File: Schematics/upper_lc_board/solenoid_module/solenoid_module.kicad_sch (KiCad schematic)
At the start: 16 parts

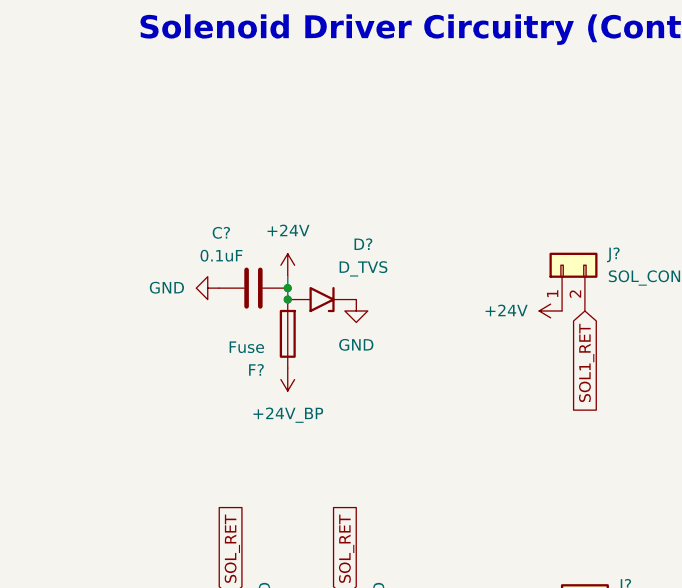
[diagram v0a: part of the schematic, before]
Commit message: update board, add new fuse
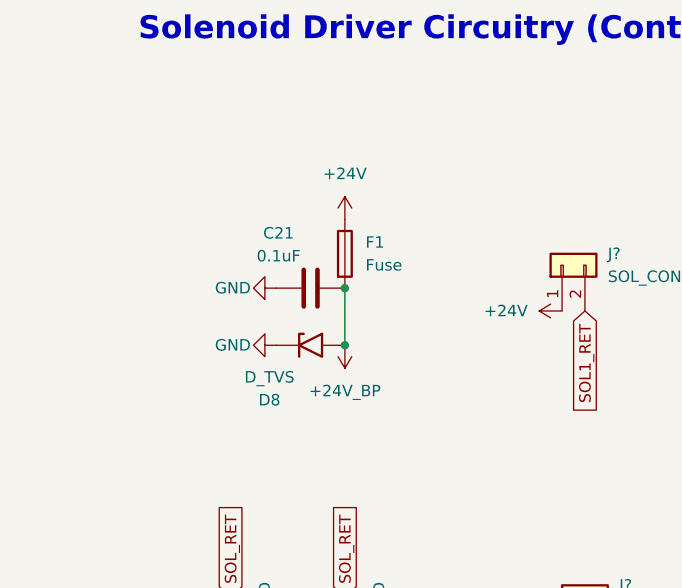
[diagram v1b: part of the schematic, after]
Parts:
- removed C?: 0.1uF, Capacitor_SMD:C_0603_1608Metric, symbol Device:C
- removed D?: D_TVS, SMBJ28A:DIOM5436X244N, symbol Diode:1.5KExxA
- removed F?: Fuse, symbol Device:Fuse
- added C21: 0.1uF, Capacitor_SMD:C_0603_1608Metric, symbol Device:C
- added D8: D_TVS, SMBJ28A:DIOM5436X244N, symbol Diode:1.5KExxA
- added F1: Fuse, symbol Device:Fuse
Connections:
- net +24V: now also F1.1
- net +24V_BP: now also C21.2, D8.2 (A2), F1.2
- net GND: now also C21.1, D8.1 (A1)

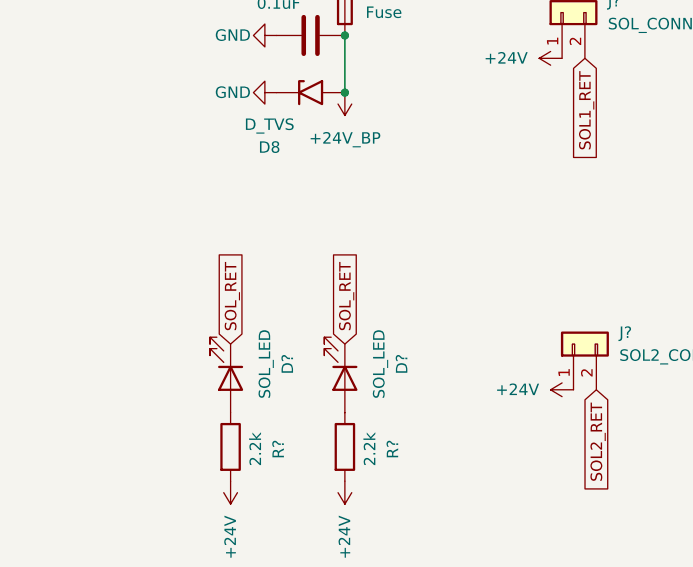
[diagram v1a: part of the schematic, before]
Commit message: update layout with new connector
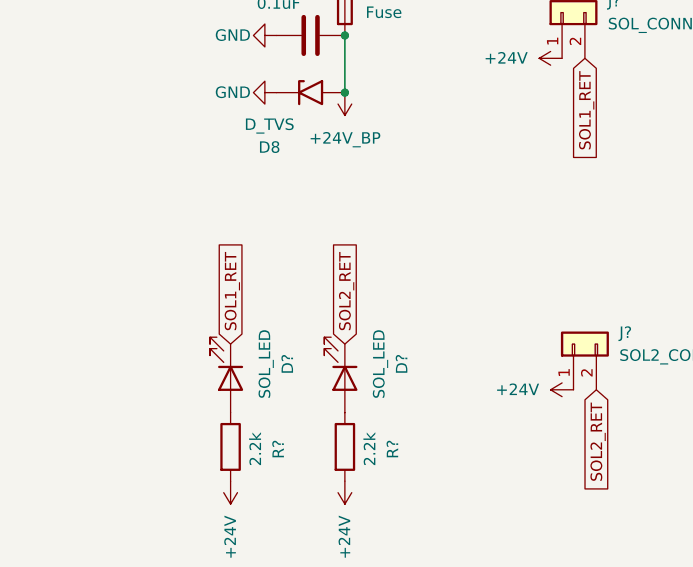
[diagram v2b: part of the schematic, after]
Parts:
- J? (x2): footprint Connector_JST:JST_EH_S2B-EH_1x02_P2.50mm_Horizontal -> 530480210:MOLEX_530480210
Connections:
- net SOL1_RET: now also D?.1 (K)
- net SOL2_RET: now also D?.1 (K)
- removed net SOL_RET: D?.1 (K), D?.1 (K)
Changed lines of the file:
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@@
 		)
 	)
-	(global_label "SOL_RET"
+	(global_label "SOL1_RET"
 		(shape input)
 		(at 25.4 85.09 90)
@@
 		)
 		(property "Intersheetrefs" "${INTERSHEET_REFS}"
-			(at 25.4 74.1825 90)
+			(at 25.4 72.973 90)
 			(effects
 				(font
@@
 		)
 	)
-	(global_label "SOL_RET"
+	(global_label "SOL2_RET"
 		(shape input)
 		(at 38.1 85.09 90)
@@
 		)
 		(property "Intersheetrefs" "${INTERSHEET_REFS}"
-			(at 38.1 74.1825 90)
+			(at 38.1 72.973 90)
 			(effects
 				(font
@@
 			)
 		)
-		(property "Footprint" "Connector_JST:JST_EH_S2B-EH_1x02_P2.50mm_Horizontal"
+		(property "Footprint" "530480210:MOLEX_530480210"
 			(at 62.23 48.26 0)
 			(effects
@@
 			)
 		)
-		(property "Footprint" "Connector_JST:JST_EH_S2B-EH_1x02_P2.50mm_Horizontal"
+		(property "Footprint" "530480210:MOLEX_530480210"
 			(at 63.5 85.09 0)
 			(effects

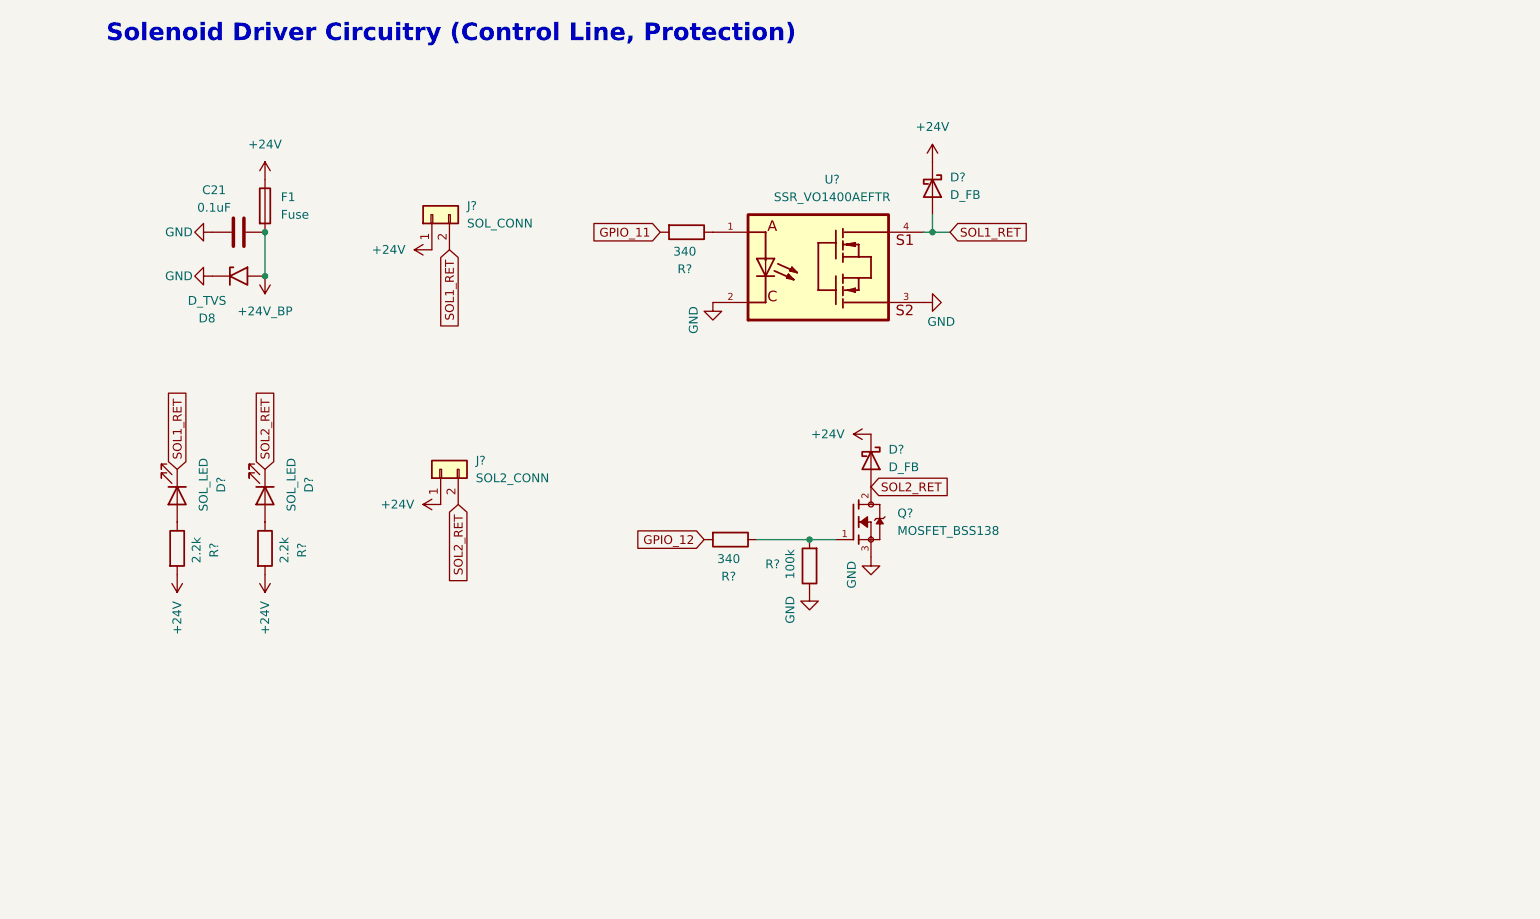
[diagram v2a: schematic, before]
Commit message: start redesigning ADC circuitry, organize schematic files. adding OPAMPS for buffered voltage divider on HALL & on PTs. layout to be adjusted after.
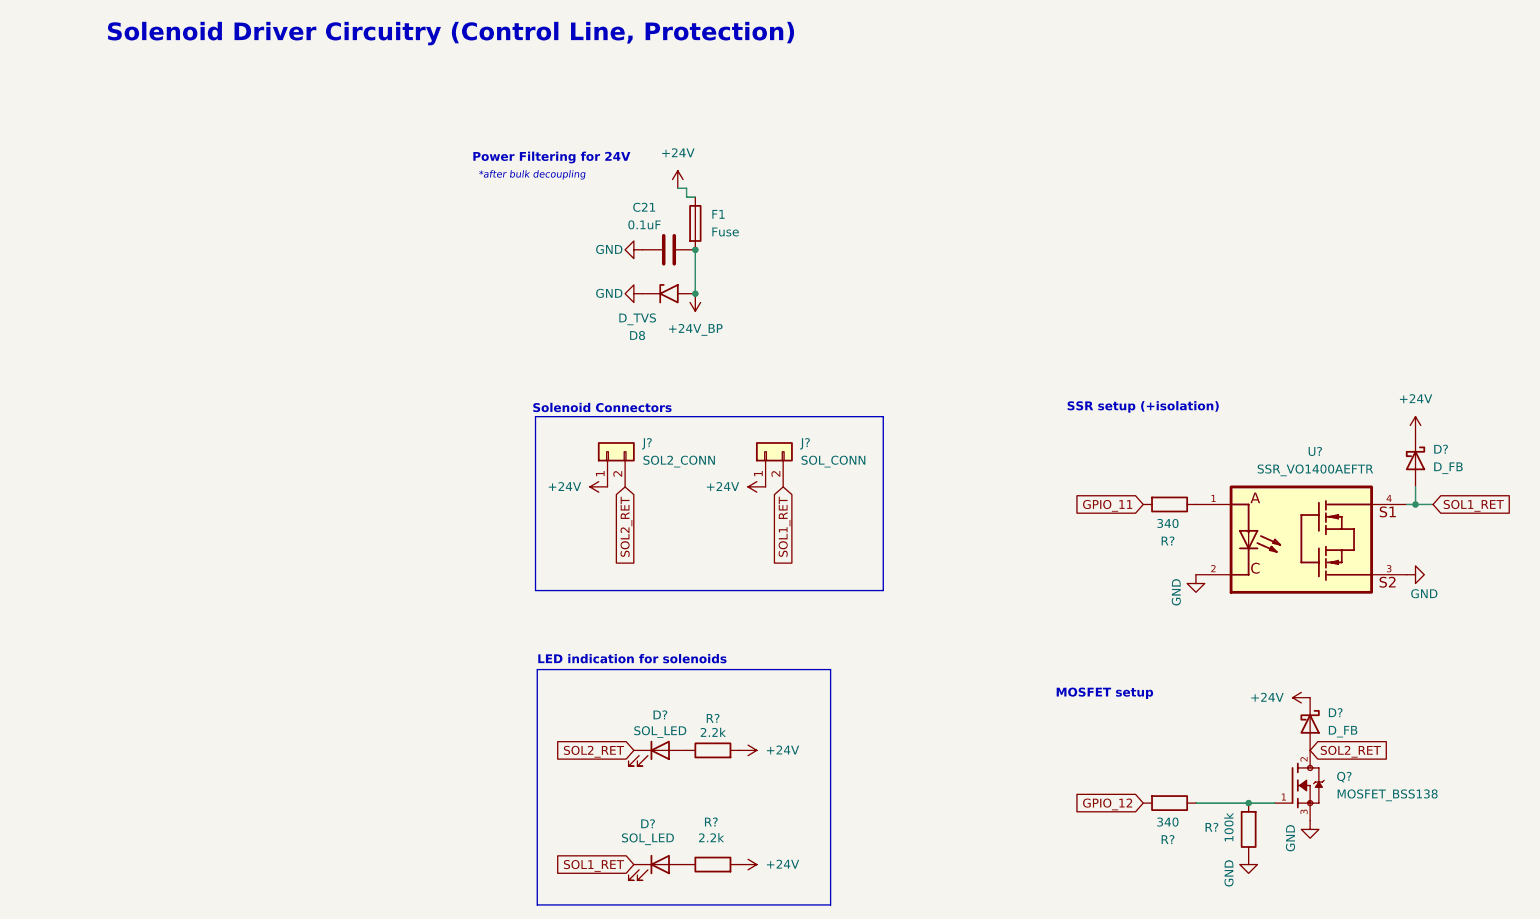
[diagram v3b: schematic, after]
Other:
- note added: "*after bulk decoupling"
- note added: "LED indication for solenoids"
- note added: "MOSFET setup"
- note added: "Power Filtering for 24V"
- note added: "SSR setup (+isolation)"
- note added: "Solenoid Connectors"
- moved on the sheet: C21, D8, D?, F1, J?, Q?, R?, U?

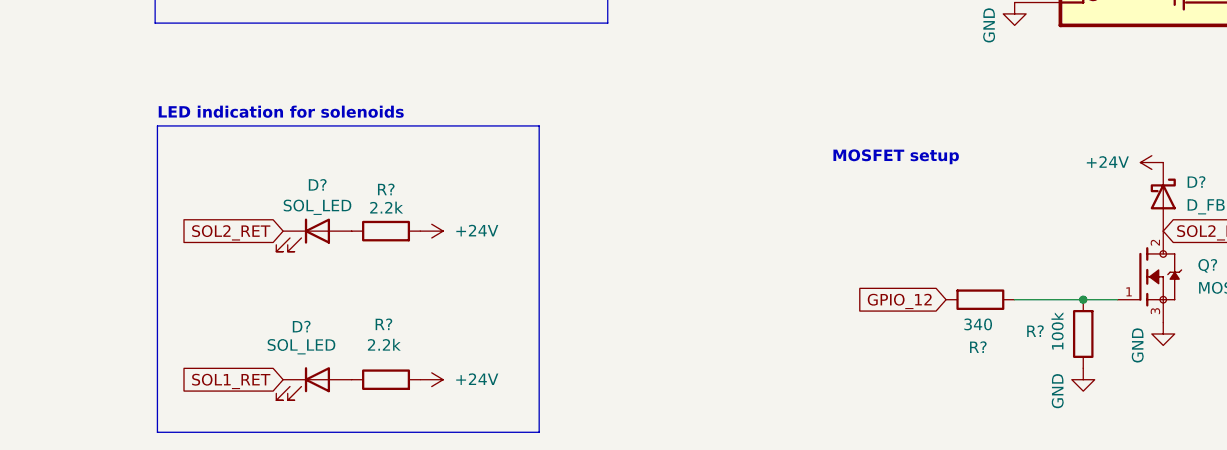
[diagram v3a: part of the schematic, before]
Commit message: solenoid schematic review, reveiewing sensors and ESP-breakout next, then finalizing layout
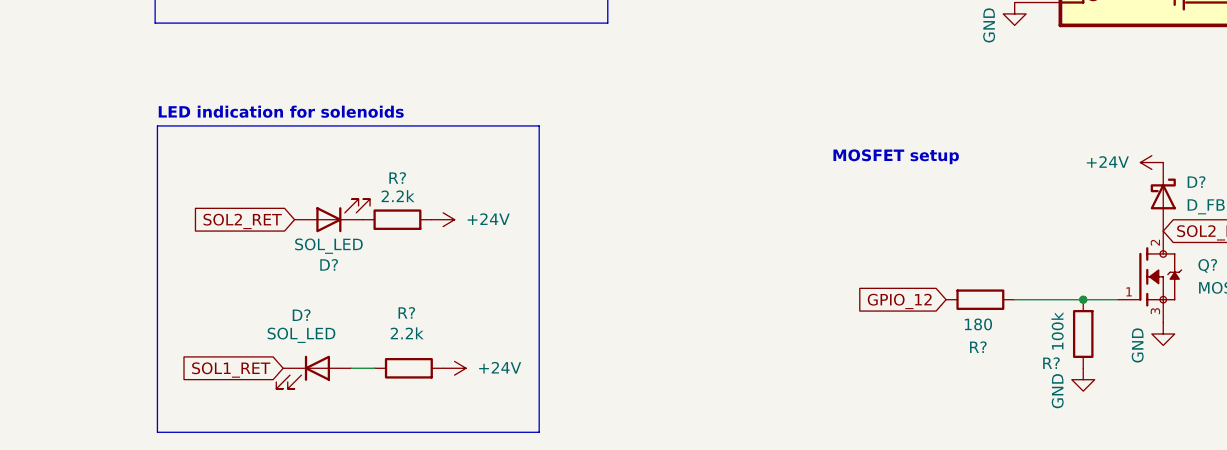
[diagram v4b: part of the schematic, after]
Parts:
- R?: value 340 -> 180
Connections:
- net SOL2_RET: now also D?.2 (A); no longer D?.1 (K)
- net at R?.1: now also D?.1 (K); no longer D?.2 (A)
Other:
- moved on the sheet: D?, R?
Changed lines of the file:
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@@
+	(wire
+		(pts
+			(xy 101.6 140.97) (xy 99.06 140.97)
+		)
+		(stroke
+			(width 0)
+			(type default)
+		)
+	)
 	(wire
 		(pts
@@
 	(global_label "SOL1_RET"
 		(shape input)
-		(at 91.44 142.24 180)
+		(at 91.44 140.97 180)
 		(fields_autoplaced yes)
 		(effects
@@
 		)
 		(property "Intersheetrefs" "${INTERSHEET_REFS}"
-			(at 79.323 142.24 0)
+			(at 79.323 140.97 0)
 			(effects
 				(font
@@
 	(global_label "SOL2_RET"
 		(shape input)
-		(at 91.44 125.73 180)
+		(at 92.71 124.46 180)
 		(fields_autoplaced yes)
 		(effects
@@
 		)
 		(property "Intersheetrefs" "${INTERSHEET_REFS}"
-			(at 79.323 125.73 0)
+			(at 80.593 124.46 0)
 			(effects
 				(font
@@
 	(symbol
 		(lib_id "Device:LED")
-		(at 95.25 125.73 0)
+		(at 96.52 124.46 180)
 		(unit 1)
 		(exclude_from_sim no)
@@
 		(dnp no)
 		(property "Reference" "D?"
-			(at 95.25 120.65 0)
+			(at 96.52 129.54 0)
 			(effects
 				(font
@@
 		)
 		(property "Value" "SOL_LED"
-			(at 95.25 122.936 0)
+			(at 96.52 127.254 0)
 			(effects
 				(font
@@
 		)
 		(property "Footprint" "LED_SMD:LED_0805_2012Metric"
-			(at 95.25 125.73 0)
+			(at 96.52 124.46 0)
 			(effects
 				(font
@@
 		)
 		(property "Datasheet" "~"
-			(at 95.25 125.73 0)
+			(at 96.52 124.46 0)
 			(effects
 				(font
@@
 		)
 		(property "Description" "Light emitting diode"
-			(at 95.25 125.73 0)
+			(at 96.52 124.46 0)
 			(effects
 				(font
@@
 	(symbol
 		(lib_id "power:+24V")
-		(at 106.68 125.73 270)
+		(at 107.95 124.46 270)
 		(unit 1)
 		(exclude_from_sim no)
@@
 		(fields_autoplaced yes)
 		(property "Reference" "#PWR?"
-			(at 102.87 125.73 0)
+			(at 104.14 124.46 0)
 			(effects
 				(font
@@
 		)
 		(property "Value" "+24V"
-			(at 110.49 125.7301 90)
+			(at 111.76 124.4601 90)
 			(effects
 				(font
@@
 		)
 		(property "Footprint" ""
-			(at 106.68 125.73 0)
+			(at 107.95 124.46 0)
 			(effects
 				(font
@@
 		)
 		(property "Datasheet" ""
-			(at 106.68 125.73 0)
+			(at 107.95 124.46 0)
 			(effects
 				(font
@@
 		)
 		(property "Description" "Power symbol creates a global label with name \"+24V\""
-			(at 106.68 125.73 0)
+			(at 107.95 124.46 0)
 			(effects
 				(font
@@
 	(symbol
 		(lib_id "Device:R")
-		(at 102.87 142.24 90)
+		(at 105.41 140.97 90)
 		(unit 1)
 		(exclude_from_sim no)
@@
 		(dnp no)
 		(property "Reference" "R?"
-			(at 102.616 136.144 90)
+			(at 105.156 134.874 90)
 			(effects
 				(font
@@
 		)
 		(property "Value" "2.2k"
-			(at 102.616 138.43 90)
+			(at 105.156 137.16 90)
 			(effects
 				(font
@@
 		)
 		(property "Footprint" "Resistor_SMD:R_1210_3225Metric"
-			(at 102.87 144.018 90)
+			(at 105.41 142.748 90)
 			(effects
 				(font
@@
 		)
 		(property "Datasheet" "~"
-			(at 102.87 142.24 0)
+			(at 105.41 140.97 0)
 			(effects
 				(font
@@
 		)
 		(property "Description" "Current Limiting Resistor"
-			(at 102.87 142.24 0)
+			(at 105.41 140.97 0)
 			(effects
 				(font
@@
 	(symbol
 		(lib_id "power:+24V")
-		(at 106.68 142.24 270)
+		(at 109.22 140.97 270)
 		(unit 1)
 		(exclude_from_sim no)
@@
 		(fields_autoplaced yes)
 		(property "Reference" "#PWR?"
-			(at 102.87 142.24 0)
+			(at 105.41 140.97 0)
 			(effects
 				(font
@@
 		)
 		(property "Value" "+24V"
-			(at 110.49 142.2401 90)
+			(at 113.03 140.9701 90)
 			(effects
 				(font
@@
 		)
 		(property "Footprint" ""
-			(at 106.68 142.24 0)
+			(at 109.22 140.97 0)
 			(effects
 				(font
@@
 		)
 		(property "Datasheet" ""
-			(at 106.68 142.24 0)
+			(at 109.22 140.97 0)
 			(effects
 				(font
@@
 		)
 		(property "Description" "Power symbol creates a global label with name \"+24V\""
-			(at 106.68 142.24 0)
+			(at 109.22 140.97 0)
 			(effects
 				(font
@@
 		(dnp no)
 		(property "Reference" "R?"
-			(at 175.006 136.906 0)
+			(at 176.784 140.462 0)
 			(effects
 				(font
@@
 			)
 		)
-		(property "Value" "340"
+		(property "Value" "180"
 			(at 168.656 136.144 90)
 			(effects
@@
 	(symbol
 		(lib_id "Device:R")
-		(at 102.87 125.73 90)
+		(at 104.14 124.46 90)
 		(unit 1)
 		(exclude_from_sim no)
@@
 		(dnp no)
 		(property "Reference" "R?"
-			(at 102.87 121.158 90)
+			(at 104.14 119.888 90)
 			(effects
 				(font
@@
 		)
 		(property "Value" "2.2k"
-			(at 102.87 123.19 90)
+			(at 104.14 121.92 90)
 			(effects
 				(font
@@
 		)
 		(property "Footprint" "Resistor_SMD:R_1210_3225Metric"
-			(at 102.87 127.508 90)
+			(at 104.14 126.238 90)
 			(effects
 				(font
@@
 		)
 		(property "Datasheet" "~"
-			(at 102.87 125.73 0)
+			(at 104.14 124.46 0)
 			(effects
 				(font
@@
 		)
 		(property "Description" "Current Limiting Resistor"
-			(at 102.87 125.73 0)
+			(at 104.14 124.46 0)
 			(effects
 				(font
@@
 	(symbol
 		(lib_id "Device:LED")
-		(at 95.25 142.24 0)
+		(at 95.25 140.97 0)
 		(unit 1)
 		(exclude_from_sim no)
@@
 		(dnp no)
 		(property "Reference" "D?"
-			(at 93.472 136.398 0)
+			(at 93.472 135.128 0)
 			(effects
 				(font
@@
 		)
 		(property "Value" "SOL_LED"
-			(at 93.472 138.43 0)
+			(at 93.472 137.16 0)
 			(effects
 				(font
@@
 		)
 		(property "Footprint" "LED_SMD:LED_0805_2012Metric"
-			(at 95.25 142.24 0)
+			(at 95.25 140.97 0)
 			(effects
 				(font
@@
 		)
 		(property "Datasheet" "~"
-			(at 95.25 142.24 0)
+			(at 95.25 140.97 0)
 			(effects
 				(font
@@
 		)
 		(property "Description" "Light emitting diode"
-			(at 95.25 142.24 0)
-			(effects
-				(font
+			(at 95.25 140.97 0)
+			(effects
+				(font
